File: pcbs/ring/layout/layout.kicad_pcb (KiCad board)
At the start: 2 copper layers, 56 x 6.2 mm, 60 parts, among them J1 ?, Q1 CSD13380F3T, Q2 CSD13380F3T, U1 BQ27427YZFR, U2 BQ29700, U3 nRF52833-QDAA, U4 MAX30102EFD+T, U5 LSM6DSOX, U6 ?, U7 TMP117AIDRVR, U8 TPS7A2018PDQN, Y1 8J32076001, Y2 3110M4-32.768DTTLLLL

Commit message: reorganized for v2
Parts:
- removed D1: ESD9B5.0ST5G, D_SOD-923:D_SOD-923
- removed TP2, TP5: , TestPoint_Pad_D2.0mm:TestPoint_Pad_D2.0mm
- removed TP3, TP4, TP6: , TestPoint_Pad_D1.0mm:TestPoint_Pad_D1.0mm
- moved TP1 10.8 mm to (136.6, 81.2)
- moved C22 6.91 mm to (148.1, 85.2), turned to 90 degrees
- moved C26 5.87 mm to (147.9, 80.7), turned to 180 degrees
- moved C23 5.21 mm to (152.3, 85.2)
- moved R1 5.01 mm to (149.2, 82.8)
- moved C24 4.27 mm to (153.6, 85.5), turned to 0 degrees
- moved U5 4.18 mm to (150.2, 84.7), turned to 0 degrees
- moved U7 3.69 mm to (150.0, 81.2), turned to 180 degrees
- moved MK1 3.40 mm to (153.8, 82.2), turned to 90 degrees
- moved R2 2.86 mm to (150.7, 82.8), turned to 180 degrees
- moved C15 2.25 mm to (147.4, 83.4)
- moved C25 1.57 mm to (151.7, 82.5), turned to 90 degrees
- moved C6 0.42 mm to (147.2, 85.1), turned to 90 degrees
- moved C11 0.38 mm to (146.3, 83.8), turned to -90 degrees
- moved L2 0.22 mm to (147.7, 82.1)
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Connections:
- U3 pad 14: hbt_int -> mic_data
- U3 pad 15: mic_data -> mic_clk
- U3 pad 17: mic_clk -> tmp_int
- U3 pad 31: tmp_int -> imu_int2
- U3 pad 4: sda -> scl
- U3 pad 5: scl -> sda
- U3 pad 7: imu_int2 -> hbt_int
- U7 pad 4: GND -> VDD
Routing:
- net VDD: track 81.8 -> 74.4 mm
- net VBATT: track 21.4 -> 14.1 mm, vias 6 -> 2
- net GND: track 35.7 -> 29.0 mm, vias 68 -> 46
- net imu_int1: track 17.1 -> 11.7 mm
- net cpu.dec4_6: track 18.2 -> 15.2 mm
- net bat_low: track 26.1 -> 24.1 mm
- net mic_clk: track 13.2 -> 15.0 mm
- net mic_data: track 12.2 -> 13.9 mm
- net rst: track 7.31 -> 5.69 mm
- net scl: track 26.9 -> 28.2 mm
- net battery.bat_vss: track 6.31 -> 5.24 mm
- net sda: track 27.2 -> 27.8 mm
- net tmp_int: track 11.5 -> 12.1 mm
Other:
- board size 56 x 6.2 mm -> 49.6 x 6.2 mm

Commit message: change to 3v3
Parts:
- U8: value TPS7A2018PDQN -> TPS7A2033PDQNR

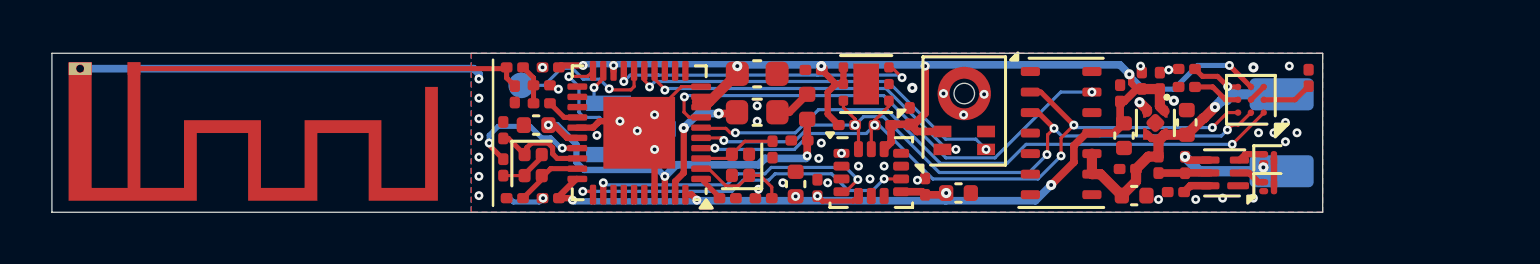
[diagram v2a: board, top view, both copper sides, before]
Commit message: smaller batmon courtyard
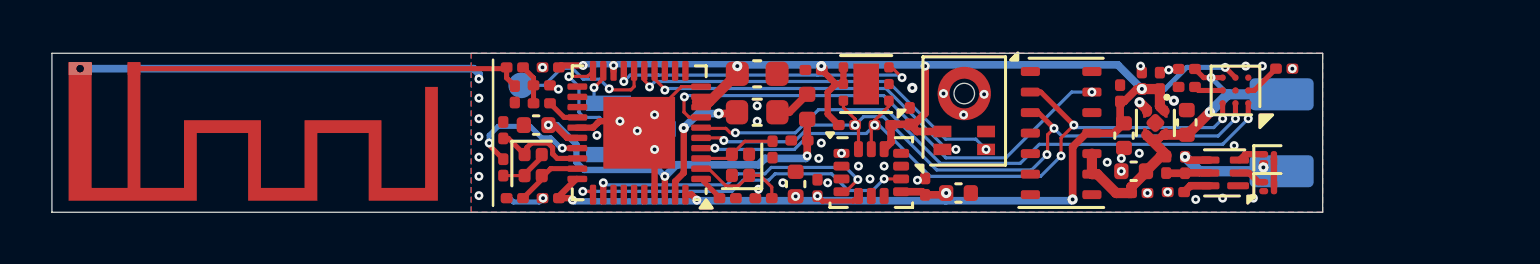
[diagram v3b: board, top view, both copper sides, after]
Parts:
- moved C19 1.04 mm to (160.7, 85.5), turned to 0 degrees
- moved R3 1.02 mm to (166.3, 80.6), turned to 0 degrees
- moved C18 0.95 mm to (160.4, 84.6), turned to 180 degrees
- moved U1 0.70 mm to (164.4, 81.5)
- moved R5 0.30 mm to (161.7, 84.3)
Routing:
- net VDD: track 74.4 -> 73.5 mm
- net batman.batman_vdd_out: track 1.89 -> 1.13 mm
- net GND: track 29.0 -> 28.3 mm, vias 46 -> 48
- net batman.bin: track 1.97 -> 1.43 mm

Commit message: temp
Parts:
- removed C27: 1uF, C_0402_1005Metric:C_0402_1005Metric
- removed C28, C29: 1uF, C_0201_0603Metric:C_0201_0603Metric
- removed the C3 at (162.4, 84.4)
- removed Q1, Q2: CSD13380F3T, Texas_PicoStar_DFN-3_0.69x0.60mm:Texas_PicoStar_DFN-3_0.69x0.60mm
- removed R4: 2.2k, R_0201_0603Metric:R_0201_0603Metric
- removed R5: 330, R_0201_0603Metric:R_0201_0603Metric
- removed the U2 at (164.0, 84.7)
- removed U8: TPS7A2033PDQNR, Texas_X2SON-4_1x1mm_P0.65mm:Texas_X2SON-4_1x1mm_P0.65mm
- renumbered C11 to C10, C12 to C11, C13 to C12, C14 to C13, C15 to C14, C16 to C15, C17 to C16, C18 to C17, C19 to C18, C20 to C19, C21 to C20, C22 to C21, C23 to C22, C24 to C23, C25 to C24, C26 to C25, C4 to C3, C5 to C4, C6 to C5, C7 to C6, C8 to C7, C9 to C8, C10 to C9, U3 to U2, U4 to U3, U5 to U4, U6 to U5, U7 to U6
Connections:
- BT1 pad 2: battery.bat_vss -> battery.vss
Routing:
- net VDD: track 73.5 -> 65.3 mm, vias 13 -> 11
- net battery.bat_vss: track 5.24 -> 0.00 mm, vias 2 -> 0
- net VBATT: track 14.1 -> 9.00 mm, vias 2 -> 1
- net battery.bat2: track 1.72 -> 0.00 mm
- net battery.bat_vm: track 1.11 -> 0.00 mm
- net battery.bat_cout: track 1.10 -> 0.00 mm
- net battery.bat_qm: track 1.09 -> 0.00 mm
- net battery.bat_dout: track 1.04 -> 0.00 mm
- net mic_data: track 13.9 -> 14.5 mm
- net GND: track 28.3 -> 27.8 mm, vias 48 -> 37
